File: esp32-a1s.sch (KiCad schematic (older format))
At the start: 7 parts

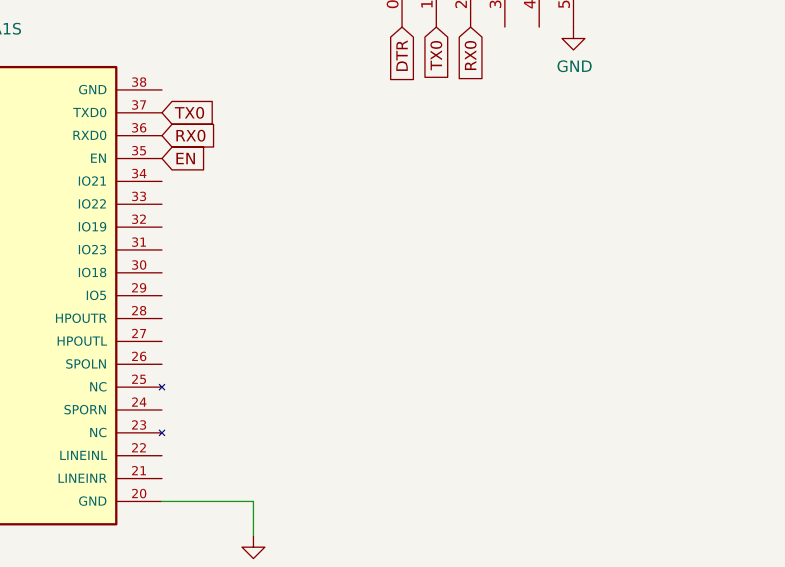
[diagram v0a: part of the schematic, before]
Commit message: added gpio
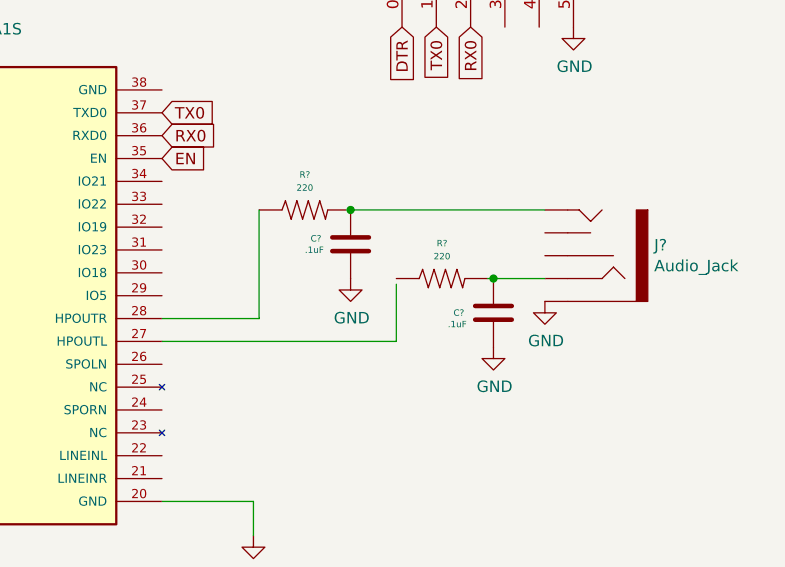
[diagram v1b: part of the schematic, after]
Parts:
- added C? (x2): .1uF, symbol Xenir:Capacitor
- added J?: Audio_Jack, symbol Xenir:Audio_Jack
- added R? (x2): 220, symbol Xenir:Resistor
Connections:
- wire segments 20 -> 27

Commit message: gg
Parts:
- C? (x2): symbol Xenir:Capacitor -> esp32-a1s-rescue:Capacitor-Xenir
- J?: symbol Xenir:Audio_Jack -> esp32-a1s-rescue:Audio_Jack-Xenir
- R? (x4): symbol Xenir:Resistor -> esp32-a1s-rescue:Resistor-Xenir
- U?: symbol Xenir:ESP32-A1S -> esp32-a1s-rescue:ESP32-A1S-Xenir
- U?: symbol Xenir:USB_to_Serial -> esp32-a1s-rescue:USB_to_Serial-Xenir
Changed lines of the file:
@@
 $EndDescr
 $Comp
-L Xenir:ESP32-A1S U?
+L esp32-a1s-rescue:ESP32-A1S-Xenir U?
 U 1 1 6287B27E
 P 5375 3325
@@
 RTS
 $Comp
-L Xenir:Resistor R?
+L esp32-a1s-rescue:Resistor-Xenir R?
 U 1 1 62884B2D
 P 2675 2925
@@
 $EndComp
 $Comp
-L Xenir:Resistor R?
+L esp32-a1s-rescue:Resistor-Xenir R?
 U 1 1 628852B4
 P 2675 3750
@@
 $EndComp
 $Comp
-L Xenir:USB_to_Serial U?
+L esp32-a1s-rescue:USB_to_Serial-Xenir U?
 U 1 1 6289875F
 P 7525 1600
@@
 $EndBitmap
 $Comp
-L Xenir:Audio_Jack J?
+L esp32-a1s-rescue:Audio_Jack-Xenir J?
 U 1 1 6289D837
 P 8050 3500
@@
 $EndComp
 $Comp
-L Xenir:Capacitor C?
+L esp32-a1s-rescue:Capacitor-Xenir C?
 U 1 1 6289EEA2
 P 7000 3100
@@
 $EndComp
 $Comp
-L Xenir:Capacitor C?
+L esp32-a1s-rescue:Capacitor-Xenir C?
 U 1 1 6289F7F9
 P 7625 3400
@@
 $EndComp
 $Comp
-L Xenir:Resistor R?
+L esp32-a1s-rescue:Resistor-Xenir R?
 U 1 1 6289FC7A
 P 7400 3250
@@
 $EndComp
 $Comp
-L Xenir:Resistor R?
+L esp32-a1s-rescue:Resistor-Xenir R?
 U 1 1 628A054A
 P 6800 2950
